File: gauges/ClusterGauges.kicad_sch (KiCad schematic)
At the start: 58 parts, among them J1 DTM06-2S nickel, 12V input (s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, J2 SWD Tag-Connect, J7 DTM06-5S nickel, CAN0 + 3x se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, Q1 PMV37ENEA automotive (AEC-Q10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, Q2 PMV37ENEA automotive (AEC-Q10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, U1 NXP S32K144 automotive (AEC-Q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, U2 LMR33630-Q1 (AEC-Q100 G1), U3 LM74700-Q1 (AEC-Q100 G1), U4 TLV733P-Q1 (AEC-Q100 G1), U5 NXP TJA1043T automotive CAN t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, U6 Raystar RFA401280B-AYW-DNF1 -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, U7 Raystar RFA401280B-AYW-DNF1 -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, U8 Raystar RFA401280B-AYW-DNF1 -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, U9 Raystar RFA401280B-AYW-DNF1 -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, Y1 8MHz (AEC-Q200)

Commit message: gauges rev B: private CAN1 link, Hall speed input, ignition input
Gateway architecture: this board is the only car-bus node and aggregates for
display/. Adds a second TCAN1044V-Q1 (CAN1, pins 51/52 from NXP's own IO
table), a 12V Hall pulse input into FTM1_CH4 (pin 58), and an ignition input
(J1 pin 3 to GPIO pin 59, pin-interrupt wake per the RM's AWIC table). Both
inputs are clamped with BAV99-Q. ERC baseline unchanged (4), routed 0
unconnected, BOM regenerated.

Co-Authored-By: Claude Sonnet 5.5 <noreply@anthropic.com>
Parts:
- added C40: 100nF VCC decouple (AEC-Q200), Capacitor_SMD:C_0603_1608Metric, symbol ClusterGauges:C_V
- added C41: 100nF VIO decouple (AEC-Q200), Capacitor_SMD:C_0603_1608Metric, symbol ClusterGauges:C_V
- added C42: 4.7nF SPLIT stabilization (AEC-Q200), Capacitor_SMD:C_0603_1608Metric, symbol ClusterGauges:C_V
- added C43: 1nF input filter (AEC-Q200), Capacitor_SMD:C_0603_1608Metric, symbol ClusterGauges:C_V
- added C44: 10nF input filter (AEC-Q200), Capacitor_SMD:C_0603_1608Metric, symbol ClusterGauges:C_V
- added D10, D11: BAV99-Q input clamp (AEC-Q101), Package_TO_SOT_SMD:SOT-23, symbol ClusterGauges:D_BAV99
- added J8: KK-254 22-27-2031, private link to display/ J3 (D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, Connector_Molex:Molex_KK-254_AE-6410-03A_1x03_P2.54mm_Vertical, symbol ClusterGauges:CONN_LINK
- added J9: KK-254 22-27-2021, Hall speed sender (signal + gr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, Connector_Molex:Molex_KK-254_AE-6410-02A_1x02_P2.54mm_Vertical, symbol ClusterGauges:CONN_SPEED
- added R40: 10k STB pulldown, normal mode while MCU resets (A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, Resistor_SMD:R_0603_1608Metric, symbol ClusterGauges:R_V
- added R41, R42: 60R split termination (AEC-Q200), Resistor_SMD:R_0603_1608Metric, symbol ClusterGauges:R_V
- added R43: 4.7k pull-up to VIN_PROT for open-collector sende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, Resistor_SMD:R_0603_1608Metric, symbol ClusterGauges:R_V
- added R44: 33k series (AEC-Q200), Resistor_SMD:R_0603_1608Metric, symbol ClusterGauges:R_V
- added R45: 15k divider bottom (AEC-Q200), Resistor_SMD:R_0603_1608Metric, symbol ClusterGauges:R_V
- added R46: 56k series (AEC-Q200), Resistor_SMD:R_0603_1608Metric, symbol ClusterGauges:R_V
- added R47: 27k divider bottom (AEC-Q200), Resistor_SMD:R_0603_1608Metric, symbol ClusterGauges:R_V
- added U10: TCAN1044V-Q1 (AEC-Q100 G1), Package_SO:SOIC-8_3.9x4.9mm_P1.27mm, symbol ClusterGauges:TCAN1044V
- J1: value DTM06-2S nickel, 12V input (sealed) -> DTM06-3S nickel, 12V input + ignition (sealed); footprint TerminalBlock_Phoenix:TerminalBlock_Phoenix_MKDS-1,5-2-5.08_1x02_P5.08mm_Horizontal -> TerminalBlock_Phoenix:TerminalBlock_Phoenix_MKDS-1,5-3-5.08_1x03_P5.08mm_Horizontal
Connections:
- net +3V3: now also C41.1, D10.2 (K2), D11.2 (K2), U10.5 (VIO)
- net +5V: now also C40.1, U10.3 (VCC)
- net GND: now also C40.2, C41.2, C42.2, C43.2, C44.2, D10.1 (A1), D11.1 (A1), J8.3 (GND), J9.2 (GND), R40.2, R45.2, R47.2, U10.2 (GND)
- net VIN_PROT: now also R43.1
- new net CAN1_H: J8.1 (CAN1_H), R41.1, U10.7 (CANH)
- new net CAN1_L: J8.2 (CAN1_L), R42.2, U10.6 (CANL)
- new net CAN1_RX: U1.52 (CAN1_RX), U10.4 (RXD)
- new net CAN1_SPLIT: C42.1, R41.2, R42.1
- new net CAN1_STB: R40.1, U1.60 (CAN1_STB), U10.8 (STB)
- new net CAN1_TX: U1.51 (CAN1_TX), U10.1 (TXD)
- new net IGN_RAW: J1.3 (IGN), R46.1
- new net IGN_SENSE: C44.1, D11.3 (CA), R46.2, R47.1, U1.59 (IGN_SENSE)
- new net SPEED_IN: C43.1, D10.3 (CA), R44.2, R45.1, U1.58 (SPEED_IN)
- new net SPEED_RAW: J9.1 (SPEED_SIG), R43.2, R44.1
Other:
- note added: "8. REV B (2026-09-30): gateway architecture. This board is the ONLY node on the car"
- note added: "CAN1 link (U10, J8). Added a Hall speed input (J9) and an ignition input (J1 pin 3)."
- note added: "REV B: CAN1 PRIVATE LINK TO display/ (TCAN1044V-Q1)"
- note added: "REV B: HALL SPEED INPUT (AutoMeter-type 12 V pulse sender)"
- note added: "REV B: IGNITION SENSE (STOP-mode wake)"
- note added: "See protocol/ for the message set and the plan for the reasons."
- note added: "bus (CAN0, firmware listen-only) and aggregates values for display/ over a private"

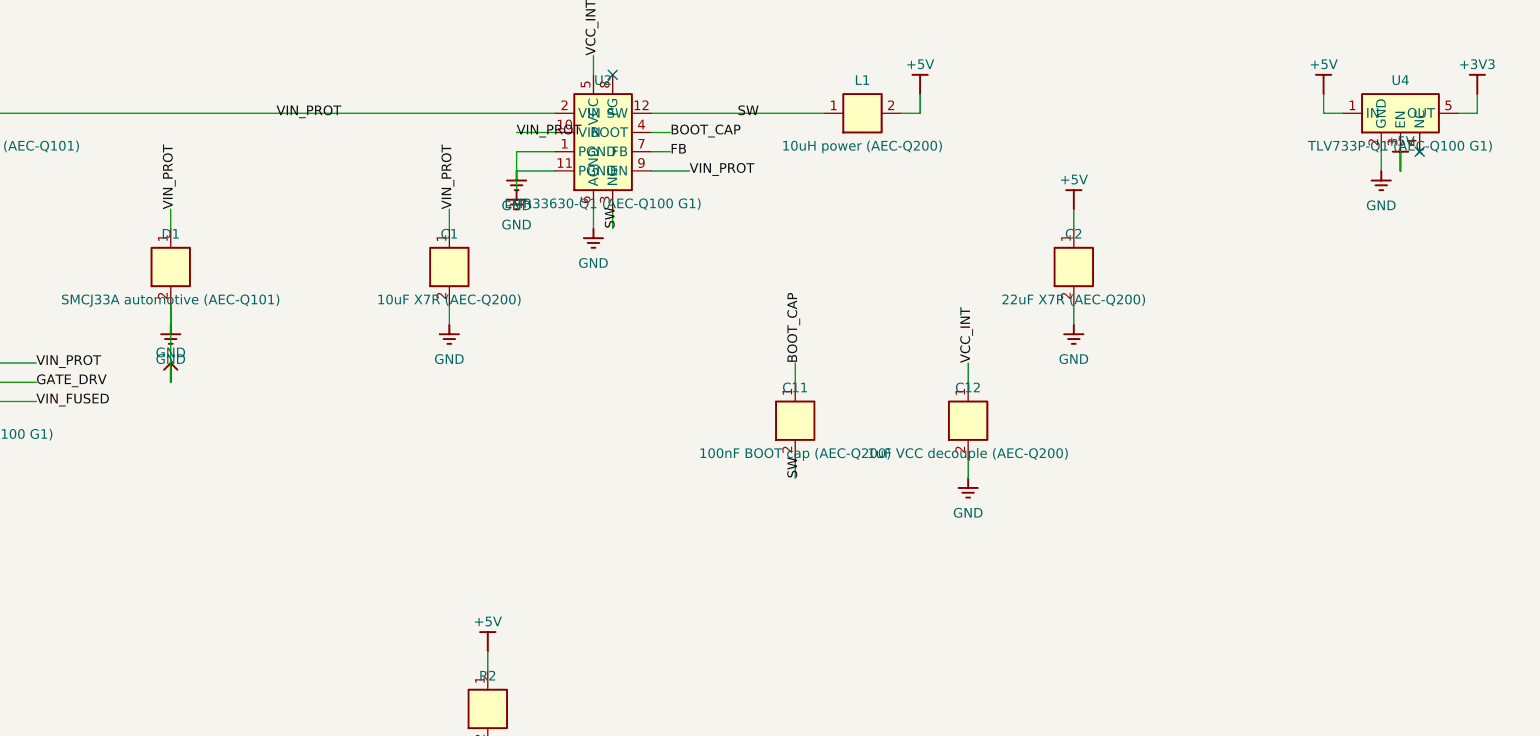
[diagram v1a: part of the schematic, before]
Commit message: Prepare both boards for fabrication: real power-stage values, orderable BOMs, fab packages
display/ power stage was placeholders inherited from fascia-pcb (RILIM, OV top,
RT, FB top...). Values are now calculated from the LM74930-Q1, LM61460-Q1 and
TLV767-Q1 datasheets, with real packages (1u XEL5030 inductor, 1206 caps, 2 mohm
sense resistor, polymer bulk cap). gauges/ buck inductor (XAL5050, Isat above the
LMR33630 current limit) and input/output capacitors fixed per its datasheet.
tools/passive_catalog.py maps every passive to a real MPN (entries flagged
verified or pattern). fab/build_fab.py writes gerbers, drill, CPL and BOM CSVs
and refuses boards with unconnected nets. Silkscreen text raised to the fab
minimum; gauges input zones moved beside the MCU. Both boards re-routed, 0
unconnected.

Co-Authored-By: Claude Sonnet 5.5 <noreply@anthropic.com>
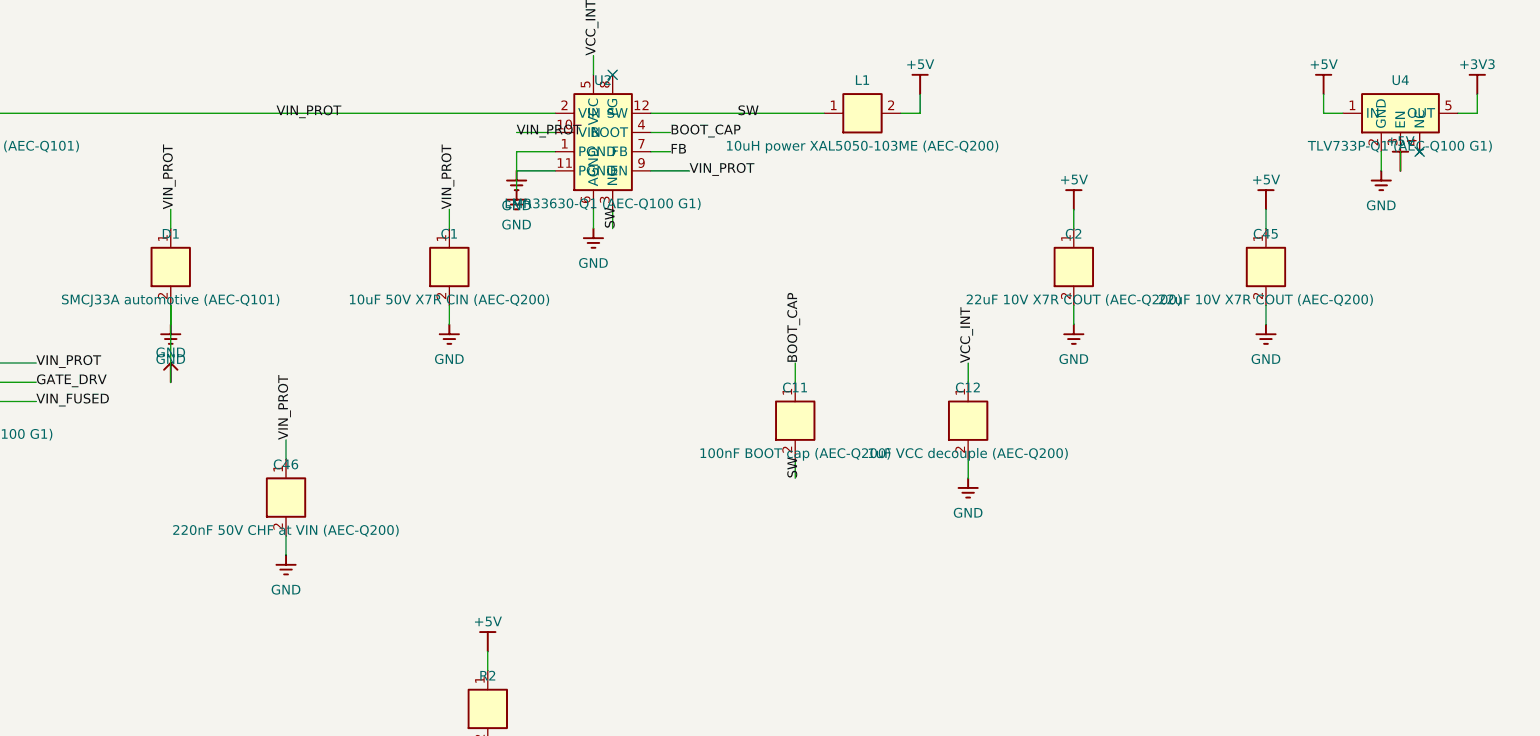
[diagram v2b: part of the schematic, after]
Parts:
- removed C1: 10uF X7R (AEC-Q200), Capacitor_SMD:C_0603_1608Metric, symbol ClusterGauges:C_V
- removed C2: 22uF X7R (AEC-Q200), Capacitor_SMD:C_0603_1608Metric, symbol ClusterGauges:C_V
- removed L1: 10uH power (AEC-Q200), Inductor_SMD:L_1210_3225Metric, symbol ClusterGauges:L_H
- removed L2: ferrite bead (AEC-Q200), Inductor_SMD:L_1210_3225Metric, symbol ClusterGauges:L_H
- added C1: 10uF 50V X7R CIN (AEC-Q200), Capacitor_SMD:C_1210_3225Metric, symbol ClusterGauges:C_1210
- added C2, C45: 22uF 10V X7R COUT (AEC-Q200), Capacitor_SMD:C_1206_3216Metric, symbol ClusterGauges:C_1206
- added C46: 220nF 50V CHF at VIN (AEC-Q200), Capacitor_SMD:C_0603_1608Metric, symbol ClusterGauges:C_V
- added L1: 10uH power XAL5050-103ME (AEC-Q200), Inductor_SMD:L_Coilcraft_XAL5050-XXX, symbol ClusterGauges:L_5050
- added L2: ferrite bead (AEC-Q200), Inductor_SMD:L_0603_1608Metric, symbol ClusterGauges:L_FB
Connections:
- net +3V3: now also L2.1
- net +5V: now also C2.1, C45.1, L1.2
- net GND: now also C1.2, C2.2, C45.2, C46.2
- net SW: now also L1.1
- net VDDA: now also L2.2
- net VIN_PROT: now also C1.1, C46.1

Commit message: Fix review findings: MOSFET pinout, gauges surge front end, converter cells, DSI
Review of 2026-10-03 found real defects; fixes and measured results:
- Nexperia PMV55ENEA/PMV37ENEA pinout is G=1, S=2, D=3: display Q1-Q3 and
  gauges Q2 had source/drain swapped. Fixed in both schematics.
- gauges/ now has the same LM74930-Q1 surge-protected front end as display/
  (5 mohm sense, OV clamp), a 5 A/32 V blade fuse on display/ (the MF-RG500 PTC
  was a 16 V part), and sender inputs with series resistor, clamp and filter.
- Converters are placed as cells around their ICs (tools/cellplace.py).
  display: SW_5V 55.6 -> 11.6 mm, boost/inverter/backlight SW 75 -> 7-13 mm,
  LM61460 input caps 57 -> 4.7-7.5 mm. gauges: SW 26.8 -> 8.7 mm, input caps 4.5 mm.
- display DSI pairs are planned by dsi_route.py after the autorouter: legs
  10.6-11.2 mm, at most 0.6 mm skew in a pair (was 64-85 mm, 21 mm skew).
- In1 is a GND plane for the router on display/ (about 925 mm of slow signals
  still cross it, down from 2615); forbidding signals there left 6-122
  connections unrouted. gauges/ keeps the old flow (planes claimed there made
  the real GND zone split into islands).
- display: USB (J13) and console UART (J12) bring-up headers, SoM and socket
  split into separate BOM lines, README rewritten.
- gauges: orderable MCU part number, DNP parts get their own BOM line and are
  left out of the placement file, 5 mohm sense resistor in the catalog.

Both boards: 0 unconnected, independent kicad-cli DRC with only accepted
categories; fab packages rebuilt. Nothing is fabricated or tested.

Co-Authored-By: Claude Sonnet 5.5 <noreply@anthropic.com>
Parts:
- removed C10: 100nF charge-pump cap (AEC-Q200), Capacitor_SMD:C_0603_1608Metric, symbol ClusterGauges:C_V
- removed Q1: PMV37ENEA automotive (AEC-Q101), Package_TO_SOT_SMD:SOT-23, symbol ClusterGauges:MOSFET_N
- removed U3: LM74700-Q1 (AEC-Q100 G1), Package_TO_SOT_SMD:SOT-23-6, symbol ClusterGauges:IC_IdealDiode
- added C47: 100nF CVS (50V), Capacitor_SMD:C_0603_1608Metric, symbol ClusterGauges:C_V
- added C48: 100nF CCAP (50V), Capacitor_SMD:C_0603_1608Metric, symbol ClusterGauges:C_V
- added C49: 100nF CTMR, Capacitor_SMD:C_0603_1608Metric, symbol ClusterGauges:C_V
- added D12: BAV99-Q fuel input clamp (AEC-Q101), Package_TO_SOT_SMD:SOT-23, symbol ClusterGauges:D_BAV99
- added D13: BAV99-Q oil input clamp (AEC-Q101), Package_TO_SOT_SMD:SOT-23, symbol ClusterGauges:D_BAV99
- added D14: BAV99-Q temp input clamp (AEC-Q101), Package_TO_SOT_SMD:SOT-23, symbol ClusterGauges:D_BAV99
- added D15: BAV99-Q battery divider clamp (AEC-Q101), Package_TO_SOT_SMD:SOT-23, symbol ClusterGauges:D_BAV99
- added Q1: PMV55ENEA ideal diode (DGATE), Package_TO_SOT_SMD:SOT-23, symbol ClusterGauges:MOSFET_N55
- added Q3: PMV55ENEA pass (HGATE), Package_TO_SOT_SMD:SOT-23, symbol ClusterGauges:MOSFET_N55
- added R48: 49.9R 1% RSET, Resistor_SMD:R_0603_1608Metric, symbol ClusterGauges:R_V
- added R49: 5m 1% sense (Susumu KRL3216E-M-R005-F-T5), Resistor_SMD:R_1206_3216Metric, symbol ClusterGauges:R_1206
- added R50: 80.6k 1% RILIM (1.5A breaker), Resistor_SMD:R_0603_1608Metric, symbol ClusterGauges:R_V
- added R51: 100k OV top, Resistor_SMD:R_0603_1608Metric, symbol ClusterGauges:R_V
- added R52: 2.05k OV bot (clamp 29.9V), Resistor_SMD:R_0603_1608Metric, symbol ClusterGauges:R_V
- added R53: 100k UV top, Resistor_SMD:R_0603_1608Metric, symbol ClusterGauges:R_V
- added R54: 11.5k UV bot (cut-off 5.5V), Resistor_SMD:R_0603_1608Metric, symbol ClusterGauges:R_V
- added R55: 1k fuel ADC series (AEC-Q200), Resistor_SMD:R_0603_1608Metric, symbol ClusterGauges:R_V
- added R56: 1k oil ADC series (AEC-Q200), Resistor_SMD:R_0603_1608Metric, symbol ClusterGauges:R_V
- added R57: 1k temp ADC series (AEC-Q200), Resistor_SMD:R_0603_1608Metric, symbol ClusterGauges:R_V
- added U3: LM74930-Q1 (AEC-Q100 G1), Package_DFN_QFN:Texas_RGE0024H_VQFN-24-1EP_4x4mm_P0.5mm_EP2.7x2.7mm, symbol ClusterGauges:LM74930
- D1: value SMCJ33A automotive (AEC-Q101) -> SMCJ33A automotive (AEC-Q101) on the fused input, ahead of the LM74930
- R16: value 47R fuel pull-up, self-calculated for the sender's 10-73R range (AEC-Q200) -> 1k fuel pull-up to +3V3 (11mW at a 10R sender) (AEC-Q200)
- R17: value 47R oil pressure pull-up, self-calculated for the sender's 10-70R range (AEC-Q200) -> 1k oil pull-up to +3V3 (AEC-Q200)
- R18: value 100R coolant temp pull-up, self-calculated for the sender's 10-300R range (AEC-Q200) -> 1k coolant temp pull-up to +3V3 (AEC-Q200)
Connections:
- net +3V3: now also D12.2 (K2), D13.2 (K2), D14.2 (K2), D15.2 (K2)
- net ADC_BATT: now also D15.3 (CA)
- net ADC_FUEL: now also D12.3 (CA), R55.2; no longer J7.3 (FUEL_SENSE), R16.2
- net ADC_OIL: now also D13.3 (CA), R56.2; no longer J7.4 (OIL_SENSE), R17.2
- net ADC_TEMP: now also D14.3 (CA), R57.2; no longer J7.5 (TEMP_SENSE), R18.2
- net AUX_VLED_RTN: now also Q2.3 (D); no longer Q2.2 (S)
- net GND: now also Q2.2 (S), C47.2, C49.2, D12.1 (A1), D13.1 (A1), D14.1 (A1), D15.1 (A1), R50.2, R52.2, R54.2, U3.13 (GND); no longer Q2.3 (D)
- net VIN_FUSED: now also D1.1, C47.1, C48.2, R48.1, R49.1, U3.22 (VS), U3.6 (EN), U3.7 (MODE)
- net VIN_PROT: now also Q1.3 (D), U3.18 (ISCP), U3.24 (C); no longer D1.1
- new net CAP_CP: C48.1, U3.23 (CAP)
- new net COMMON: Q1.2 (S), Q3.2 (S), U3.15 (OUT), U3.2 (A)
- new net CS_PLUS: R48.2, U3.20 (CS+)
- new net DGATE: Q1.1 (G), U3.1 (DGATE)
- new net HGATE: Q3.1 (G), U3.14 (HGATE)
- new net ILIM: R50.1, U3.11 (ILIM)
- new net OV_DIV: R51.2, R52.1, U3.16 (OVCLAMP), U3.5 (OV)
- new net SENDER_FUEL: J7.3 (FUEL_SENSE), R16.2, R55.1
- new net SENDER_OIL: J7.4 (OIL_SENSE), R17.2, R56.1
- new net SENDER_TEMP: J7.5 (TEMP_SENSE), R18.2, R57.1
- new net SENSE_OUT: Q3.3 (D), R49.2, U3.19 (CS-)
- new net SW_SENSE: R51.1, R53.1, U3.3 (SW)
- new net TMR: C49.1, U3.9 (TMR)
- new net UVLO_DIV: R53.2, R54.1, U3.4 (UVLO)
- no-connect marks 34 -> 40
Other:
- note added: "INPUT PROTECTION: LM74930-Q1 IDEAL DIODE + OV CLAMP + CURRENT LIMIT (review fix 2026-10-03)"
